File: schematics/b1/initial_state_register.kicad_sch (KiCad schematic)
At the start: 18 parts, among them SW1 SW_SPDT, SW2 SW_SPDT, SW3 SW_SPDT, SW4 SW_SPDT, SW5 SW_SPDT, SW6 SW_SPDT, SW7 SW_SPDT, SW8 SW_Push, U1 74HC165

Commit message: Added schematic page for the status block.
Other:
- company: (none) -> shawnd.xyz
- title: B1 -> Initial State Register
- moved on the sheet: C1
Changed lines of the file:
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@@
   (paper "A4")
   (title_block
-    (title "B1")
-    (date "2024-02-01")
+    (title "Initial State Register")
+    (date "2024-02-05")
     (rev "1")
+    (company "shawnd.xyz")
     (comment 2 "clear EEPROM memory if high at boot time.")
     (comment 3 "configure the unit ID by toggling the DIP switches. There is also a reset button that will")
@@
     (stroke (width 0) (type default))
   )
-  (wire (pts (xy 170.18 34.29) (xy 189.23 34.29))
+  (wire (pts (xy 170.18 34.29) (xy 185.42 34.29))
     (stroke (width 0) (type default))
   )
@@
     (stroke (width 0) (type default))
   )
-  (wire (pts (xy 189.23 43.18) (xy 189.23 44.45))
-    (stroke (width 0) (type default))
-  )
   (wire (pts (xy 125.73 133.35) (xy 138.43 133.35))
     (stroke (width 0) (type default))
@@
     (stroke (width 0) (type default))
   )
-  (wire (pts (xy 189.23 34.29) (xy 189.23 35.56))
+  (wire (pts (xy 185.42 34.29) (xy 185.42 35.56))
     (stroke (width 0) (type default))
   )
@@
     (stroke (width 0) (type default))
   )
-  (wire (pts (xy 102.87 50.8) (xy 102.87 53.34))
+  (wire (pts (xy 102.87 52.07) (xy 102.87 53.34))
     (stroke (width 0) (type default))
   )
@@
     (stroke (width 0) (type default))
   )
-  (wire (pts (xy 105.41 171.45) (xy 105.41 168.91))
+  (wire (pts (xy 105.41 170.18) (xy 105.41 168.91))
     (stroke (width 0) (type default))
   )
@@
     (effects (font (size 1.27 1.27)) (justify left))
   )
-  (hierarchical_label "VCC" (shape input) (at 102.87 50.8 90) (fields_autoplaced)
+  (hierarchical_label "VCC" (shape input) (at 102.87 52.07 90) (fields_autoplaced)
     (effects (font (size 1.27 1.27)) (justify left))
   )
@@
     )
   )
-  (symbol (lib_id "Device:C_Polarized") (at 189.23 39.37 0) (unit 1)
+  (symbol (lib_id "Device:C_Polarized") (at 185.42 39.37 0) (unit 1)
     (in_bom yes) (on_board yes) (dnp no) (fields_autoplaced)
-    (property "Reference" "C1" (at 193.04 37.211 0)
+    (property "Reference" "C1" (at 189.23 37.211 0)
       (effects (font (size 1.27 1.27)) (justify left))
     )
-    (property "Value" "10u" (at 193.04 39.751 0)
+    (property "Value" "10u" (at 189.23 39.751 0)
       (effects (font (size 1.27 1.27)) (justify left))
     )
-    (property "Footprint" "" (at 190.1952 43.18 0)
-      (effects (font (size 1.27 1.27)) hide)
-    )
-    (property "Datasheet" "~" (at 189.23 39.37 0)
+    (property "Footprint" "" (at 186.3852 43.18 0)
+      (effects (font (size 1.27 1.27)) hide)
+    )
+    (property "Datasheet" "~" (at 185.42 39.37 0)
       (effects (font (size 1.27 1.27)) hide)
     )
@@
     )
   )
-  (symbol (lib_id "power:GND") (at 105.41 171.45 0) (unit 1)
+  (symbol (lib_id "power:GND") (at 105.41 170.18 0) (unit 1)
     (in_bom yes) (on_board yes) (dnp no) (fields_autoplaced)
-    (property "Reference" "#PWR03" (at 105.41 177.8 0)
-      (effects (font (size 1.27 1.27)) hide)
-    )
-    (property "Value" "GND" (at 105.41 176.53 0)
-      (effects (font (size 1.27 1.27)))
-    )
-    (property "Footprint" "" (at 105.41 171.45 0)
-      (effects (font (size 1.27 1.27)) hide)
-    )
-    (property "Datasheet" "" (at 105.41 171.45 0)
+    (property "Reference" "#PWR03" (at 105.41 176.53 0)
+      (effects (font (size 1.27 1.27)) hide)
+    )
+    (property "Value" "GND" (at 105.41 175.26 0)
+      (effects (font (size 1.27 1.27)))
+    )
+    (property "Footprint" "" (at 105.41 170.18 0)
+      (effects (font (size 1.27 1.27)) hide)
+    )
+    (property "Datasheet" "" (at 105.41 170.18 0)
       (effects (font (size 1.27 1.27)) hide)
     )
@@
     )
   )
-  (symbol (lib_id "power:GND") (at 189.23 44.45 0) (unit 1)
+  (symbol (lib_id "power:GND") (at 185.42 43.18 0) (unit 1)
     (in_bom yes) (on_board yes) (dnp no) (fields_autoplaced)
-    (property "Reference" "#PWR05" (at 189.23 50.8 0)
-      (effects (font (size 1.27 1.27)) hide)
-    )
-    (property "Value" "GND" (at 189.23 49.53 0)
-      (effects (font (size 1.27 1.27)))
-    )
-    (property "Footprint" "" (at 189.23 44.45 0)
-      (effects (font (size 1.27 1.27)) hide)
-    )
-    (property "Datasheet" "" (at 189.23 44.45 0)
-      (effects (font (size 1.27 1.27)) hide)
-    )
+    (property "Reference" "#PWR05" (at 185.42 49.53 0)
+      (effects (font (size 1.27 1.27)) hide)
+    )
+    (property "Value" "GND" (at 185.42 48.26 0)
+      (effects (font (size 1.27 1.27)))
+    )
+    (property "Footprint" "" (at 185.42 43.18 0)
+      (effects (font (size 1.27 1.27)) hide)
+    )
+    (property "Datasheet" "" (at 185.42 43.18 0)
+      (effects (font (size 1.27 1.27)) hide)
+    )

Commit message: Updated schematics.
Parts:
- added C6: 0.1u, symbol Device:C
- C1: value 10u -> 1u
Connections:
- net GND: now also C6.2
- net VCC: now also C6.1
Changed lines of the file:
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@@
   (junction (at 102.87 146.05) (diameter 0) (color 0 0 0 0)
+  )
+  (junction (at 199.39 44.45) (diameter 0) (color 0 0 0 0)
+  )
+  (junction (at 185.42 34.29) (diameter 0) (color 0 0 0 0)
   )
   (junction (at 102.87 99.06) (diameter 0) (color 0 0 0 0)
@@
     (stroke (width 0) (type default))
   )
+  (wire (pts (xy 199.39 44.45) (xy 199.39 43.18))
+    (stroke (width 0) (type default))
+  )
   (wire (pts (xy 102.87 130.81) (xy 102.87 115.57))
     (stroke (width 0) (type default))
@@
     (stroke (width 0) (type default))
   )
+  (wire (pts (xy 199.39 35.56) (xy 199.39 34.29))
+    (stroke (width 0) (type default))
+  )
   (wire (pts (xy 102.87 53.34) (xy 115.57 53.34))
     (stroke (width 0) (type default))
@@
     (stroke (width 0) (type default))
   )
+  (wire (pts (xy 185.42 44.45) (xy 185.42 43.18))
+    (stroke (width 0) (type default))
+  )
   (wire (pts (xy 105.41 120.65) (xy 106.68 120.65))
     (stroke (width 0) (type default))
@@
     (stroke (width 0) (type default))
   )
+  (wire (pts (xy 185.42 34.29) (xy 199.39 34.29))
+    (stroke (width 0) (type default))
+  )
   (wire (pts (xy 125.73 148.59) (xy 140.97 148.59))
     (stroke (width 0) (type default))
   )
+  (wire (pts (xy 199.39 44.45) (xy 185.42 44.45))
+    (stroke (width 0) (type default))
+  )
   (wire (pts (xy 133.35 101.6) (xy 133.35 63.5))
     (stroke (width 0) (type default))
@@
   )
   (wire (pts (xy 138.43 68.58) (xy 157.48 68.58))
+    (stroke (width 0) (type default))
+  )
+  (wire (pts (xy 199.39 45.72) (xy 199.39 44.45))
     (stroke (width 0) (type default))
   )
@@
       (effects (font (size 1.27 1.27)) (justify left))
     )
-    (property "Value" "10u" (at 189.23 39.751 0)
+    (property "Value" "1u" (at 189.23 39.751 0)
       (effects (font (size 1.27 1.27)) (justify left))
     )
@@
     )
   )
+  (symbol (lib_id "Device:C") (at 199.39 39.37 0) (unit 1)
+    (in_bom yes) (on_board yes) (dnp no) (fields_autoplaced)
+    (property "Reference" "C6" (at 203.2 38.1 0)
+      (effects (font (size 1.27 1.27)) (justify left))
+    )
+    (property "Value" "0.1u" (at 203.2 40.64 0)
+      (effects (font (size 1.27 1.27)) (justify left))
+    )
+    (property "Footprint" "" (at 200.3552 43.18 0)
+      (effects (font (size 1.27 1.27)) hide)
+    )
+    (property "Datasheet" "~" (at 199.39 39.37 0)
+      (effects (font (size 1.27 1.27)) hide)
+    )
+    (pin "2")
+    (pin "1")
+    (instances
+      (project "b1"
+        (path "/d6142fa5-2354-4512-9919-37616259c364/15951702-f191-4c4b-b68c-efdb5de618b5"
+          (reference "C6") (unit 1)
+        )
+      )
+    )
+  )
   (symbol (lib_id "Switch:SW_SPDT") (at 120.65 55.88 0) (mirror y) (unit 1)
     (in_bom yes) (on_board yes) (dnp no)
@@
     )
   )
-  (symbol (lib_id "power:GND") (at 185.42 43.18 0) (unit 1)
+  (symbol (lib_id "power:GND") (at 199.39 45.72 0) (unit 1)
     (in_bom yes) (on_board yes) (dnp no) (fields_autoplaced)
-    (property "Reference" "#PWR05" (at 185.42 49.53 0)
-      (effects (font (size 1.27 1.27)) hide)
-    )
-    (property "Value" "GND" (at 185.42 48.26 0)
-      (effects (font (size 1.27 1.27)))
-    )
-    (property "Footprint" "" (at 185.42 43.18 0)
-      (effects (font (size 1.27 1.27)) hide)
-    )
-    (property "Datasheet" "" (at 185.42 43.18 0)
-      (effects (font (size 1.27 1.27)) hide)
-    )
+    (property "Reference" "#PWR05" (at 199.39 52.07 0)
+      (effects (font (size 1.27 1.27)) hide)
+    )
+    (property "Value" "GND" (at 199.39 50.8 0)
+      (effects (font (size 1.27 1.27)))
+    )
+    (property "Footprint" "" (at 199.39 45.72 0)
+      (effects (font (size 1.27 1.27)) hide)
+    )
+    (property "Datasheet" "" (at 199.39 45.72 0)
+      (effects (font (size 1.27 1.27)) hide)
+    )

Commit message: Updated bypass capacitor values.
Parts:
- added C3: 10u, symbol Device:C_Polarized
- C1: symbol Device:C_Polarized -> Device:C
- renumbered C6 to C2
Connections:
- net GND: now also C3.2
- net VCC: now also C3.1
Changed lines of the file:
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@@
   (junction (at 102.87 115.57) (diameter 0) (color 0 0 0 0)
   )
+  (junction (at 213.36 44.45) (diameter 0) (color 0 0 0 0)
+  )
   (junction (at 102.87 130.81) (diameter 0) (color 0 0 0 0)
   )
@@
   )
   (junction (at 105.41 168.91) (diameter 0) (color 0 0 0 0)
+  )
+  (junction (at 199.39 34.29) (diameter 0) (color 0 0 0 0)
   )
   (junction (at 102.87 68.58) (diameter 0) (color 0 0 0 0)
@@
     (stroke (width 0) (type default))
   )
+  (wire (pts (xy 213.36 43.18) (xy 213.36 44.45))
+    (stroke (width 0) (type default))
+  )
   (wire (pts (xy 170.18 34.29) (xy 185.42 34.29))
     (stroke (width 0) (type default))
@@
     (stroke (width 0) (type default))
   )
+  (wire (pts (xy 213.36 44.45) (xy 199.39 44.45))
+    (stroke (width 0) (type default))
+  )
   (wire (pts (xy 105.41 104.14) (xy 105.41 120.65))
     (stroke (width 0) (type default))
@@
     (stroke (width 0) (type default))
   )
-  (wire (pts (xy 199.39 45.72) (xy 199.39 44.45))
+  (wire (pts (xy 213.36 45.72) (xy 213.36 44.45))
     (stroke (width 0) (type default))
   )
@@
     (stroke (width 0) (type default))
   )
+  (wire (pts (xy 213.36 35.56) (xy 213.36 34.29))
+    (stroke (width 0) (type default))
+  )
   (wire (pts (xy 102.87 146.05) (xy 115.57 146.05))
     (stroke (width 0) (type default))
@@
   )
   (wire (pts (xy 105.41 58.42) (xy 105.41 73.66))
+    (stroke (width 0) (type default))
+  )
+  (wire (pts (xy 213.36 34.29) (xy 199.39 34.29))
     (stroke (width 0) (type default))
   )
@@
   (symbol (lib_id "power:GND") (at 170.18 93.98 0) (unit 1)
     (in_bom yes) (on_board yes) (dnp no) (fields_autoplaced)
-    (property "Reference" "#PWR04" (at 170.18 100.33 0)
+    (property "Reference" "#PWR02" (at 170.18 100.33 0)
       (effects (font (size 1.27 1.27)) hide)
     )
@@
       (project "b1"
         (path "/d6142fa5-2354-4512-9919-37616259c364/15951702-f191-4c4b-b68c-efdb5de618b5"
-          (reference "#PWR04") (unit 1)
+          (reference "#PWR02") (unit 1)
         )
       )
@@
     )
   )
-  (symbol (lib_id "Device:C_Polarized") (at 185.42 39.37 0) (unit 1)
+  (symbol (lib_id "Device:C") (at 185.42 39.37 0) (unit 1)
     (in_bom yes) (on_board yes) (dnp no) (fields_autoplaced)
-    (property "Reference" "C1" (at 189.23 37.211 0)
+    (property "Reference" "C1" (at 189.23 38.1 0)
       (effects (font (size 1.27 1.27)) (justify left))
     )
-    (property "Value" "1u" (at 189.23 39.751 0)
+    (property "Value" "1u" (at 189.23 40.64 0)
       (effects (font (size 1.27 1.27)) (justify left))
     )
@@
   (symbol (lib_id "power:GND") (at 105.41 170.18 0) (unit 1)
     (in_bom yes) (on_board yes) (dnp no) (fields_autoplaced)
-    (property "Reference" "#PWR03" (at 105.41 176.53 0)
+    (property "Reference" "#PWR01" (at 105.41 176.53 0)
       (effects (font (size 1.27 1.27)) hide)
     )
@@
       (project "b1"
         (path "/d6142fa5-2354-4512-9919-37616259c364/15951702-f191-4c4b-b68c-efdb5de618b5"
-          (reference "#PWR03") (unit 1)
+          (reference "#PWR01") (unit 1)
         )
       )
@@
   (symbol (lib_id "Device:C") (at 199.39 39.37 0) (unit 1)
     (in_bom yes) (on_board yes) (dnp no) (fields_autoplaced)
-    (property "Reference" "C6" (at 203.2 38.1 0)
+    (property "Reference" "C2" (at 203.2 38.1 0)
       (effects (font (size 1.27 1.27)) (justify left))
     )
@@
       (project "b1"
         (path "/d6142fa5-2354-4512-9919-37616259c364/15951702-f191-4c4b-b68c-efdb5de618b5"
-          (reference "C6") (unit 1)
+          (reference "C2") (unit 1)
         )
       )
@@
     )
   )
-  (symbol (lib_id "power:GND") (at 199.39 45.72 0) (unit 1)
+  (symbol (lib_id "power:GND") (at 213.36 45.72 0) (unit 1)
     (in_bom yes) (on_board yes) (dnp no) (fields_autoplaced)
-    (property "Reference" "#PWR05" (at 199.39 52.07 0)
-      (effects (font (size 1.27 1.27)) hide)
-    )
-    (property "Value" "GND" (at 199.39 50.8 0)
-      (effects (font (size 1.27 1.27)))
-    )
-    (property "Footprint" "" (at 199.39 45.72 0)
-      (effects (font (size 1.27 1.27)) hide)
-    )
-    (property "Datasheet" "" (at 199.39 45.72 0)
-      (effects (font (size 1.27 1.27)) hide)
-    )
-    (pin "1")
-    (instances
-      (project "b1"
-        (path "/d6142fa5-2354-4512-9919-37616259c364/15951702-f191-4c4b-b68c-efdb5de618b5"
-          (reference "#PWR05") (unit 1)
+    (property "Reference" "#PWR03" (at 213.36 52.07 0)
+      (effects (font (size 1.27 1.27)) hide)
+    )
+    (property "Value" "GND" (at 213.36 50.8 0)
+      (effects (font (size 1.27 1.27)))
+    )
+    (property "Footprint" "" (at 213.36 45.72 0)
+      (effects (font (size 1.27 1.27)) hide)
+    )
+    (property "Datasheet" "" (at 213.36 45.72 0)
+      (effects (font (size 1.27 1.27)) hide)
+    )
+    (pin "1")
+    (instances
+      (project "b1"
+        (path "/d6142fa5-2354-4512-9919-37616259c364/15951702-f191-4c4b-b68c-efdb5de618b5"
+          (reference "#PWR03") (unit 1)
         )
       )
@@
         )
       )
+    )
+  )
+  (symbol (lib_id "Device:C_Polarized") (at 213.36 39.37 0) (unit 1)
+    (in_bom yes) (on_board yes) (dnp no)
+    (property "Reference" "C3" (at 217.17 38.1 0)
+      (effects (font (size 1.27 1.27)) (justify left))
+    )
+    (property "Value" "10u" (at 217.17 40.64 0)
+      (effects (font (size 1.27 1.27)) (justify left))
+    )
+    (property "Footprint" "" (at 214.3252 43.18 0)
+      (effects (font (size 1.27 1.27)) hide)
+    )
+    (property "Datasheet" "~" (at 213.36 39.37 0)
+      (effects (font (size 1.27 1.27)) hide)
+    )
+    (pin "2")
+    (pin "1")
+    (instances
+      (project "b1"
+        (path "/d6142fa5-2354-4512-9919-37616259c364/15951702-f191-4c4b-b68c-efdb5de618b5"
+          (reference "C3") (unit 1)
+        )
+      )

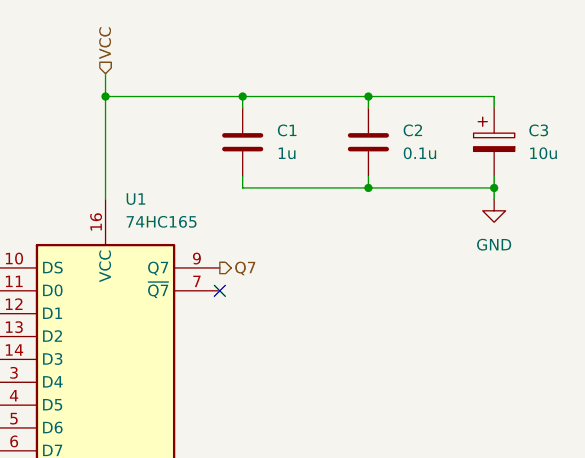
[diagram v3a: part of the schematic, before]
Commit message: Added schematic page for LoRa.
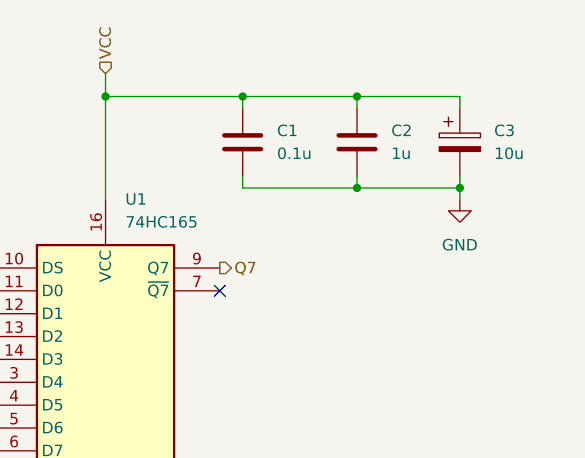
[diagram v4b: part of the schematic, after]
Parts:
- C1: value 1u -> 0.1u
- C2: value 0.1u -> 1u
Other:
- moved on the sheet: C2, C3
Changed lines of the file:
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@@
   (title_block
     (title "Initial State Register")
-    (date "2024-02-05")
+    (date "2024-02-06")
     (rev "1")
     (company "shawnd.xyz")
@@
     (comment 4 "The initial state register is used to read a B1 unit's ID upon first boot. The user can")
   )
+  (junction (at 198.12 44.45) (diameter 0) (color 0 0 0 0)
+  )
   (junction (at 105.41 73.66) (diameter 0) (color 0 0 0 0)
   )
   (junction (at 102.87 53.34) (diameter 0) (color 0 0 0 0)
   )
+  (junction (at 209.55 44.45) (diameter 0) (color 0 0 0 0)
+  )
   (junction (at 105.41 151.13) (diameter 0) (color 0 0 0 0)
   )
+  (junction (at 198.12 34.29) (diameter 0) (color 0 0 0 0)
+  )
   (junction (at 102.87 115.57) (diameter 0) (color 0 0 0 0)
   )
-  (junction (at 213.36 44.45) (diameter 0) (color 0 0 0 0)
-  )
   (junction (at 102.87 130.81) (diameter 0) (color 0 0 0 0)
   )
@@
   (junction (at 102.87 146.05) (diameter 0) (color 0 0 0 0)
   )
-  (junction (at 199.39 44.45) (diameter 0) (color 0 0 0 0)
-  )
   (junction (at 185.42 34.29) (diameter 0) (color 0 0 0 0)
   )
@@
   )
   (junction (at 105.41 168.91) (diameter 0) (color 0 0 0 0)
-  )
-  (junction (at 199.39 34.29) (diameter 0) (color 0 0 0 0)
   )
   (junction (at 102.87 68.58) (diameter 0) (color 0 0 0 0)
@@
     (stroke (width 0) (type default))
   )
-  (wire (pts (xy 199.39 44.45) (xy 199.39 43.18))
+  (wire (pts (xy 198.12 44.45) (xy 198.12 43.18))
     (stroke (width 0) (type default))
   )
@@
     (stroke (width 0) (type default))
   )
-  (wire (pts (xy 213.36 43.18) (xy 213.36 44.45))
+  (wire (pts (xy 209.55 43.18) (xy 209.55 44.45))
     (stroke (width 0) (type default))
   )
@@
     (stroke (width 0) (type default))
   )
-  (wire (pts (xy 199.39 35.56) (xy 199.39 34.29))
+  (wire (pts (xy 198.12 35.56) (xy 198.12 34.29))
     (stroke (width 0) (type default))
   )
@@
     (stroke (width 0) (type default))
   )
+  (wire (pts (xy 198.12 44.45) (xy 209.55 44.45))
+    (stroke (width 0) (type default))
+  )
   (wire (pts (xy 127 168.91) (xy 127 163.83))
     (stroke (width 0) (type default))
@@
     (stroke (width 0) (type default))
   )
-  (wire (pts (xy 213.36 44.45) (xy 199.39 44.45))
-    (stroke (width 0) (type default))
-  )
   (wire (pts (xy 105.41 104.14) (xy 105.41 120.65))
     (stroke (width 0) (type default))
@@
     (stroke (width 0) (type default))
   )
-  (wire (pts (xy 185.42 34.29) (xy 199.39 34.29))
+  (wire (pts (xy 185.42 34.29) (xy 198.12 34.29))
     (stroke (width 0) (type default))
   )
@@
     (stroke (width 0) (type default))
   )
-  (wire (pts (xy 199.39 44.45) (xy 185.42 44.45))
-    (stroke (width 0) (type default))
-  )
   (wire (pts (xy 133.35 101.6) (xy 133.35 63.5))
     (stroke (width 0) (type default))
@@
     (stroke (width 0) (type default))
   )
-  (wire (pts (xy 213.36 45.72) (xy 213.36 44.45))
+  (wire (pts (xy 209.55 45.72) (xy 209.55 44.45))
+    (stroke (width 0) (type default))
+  )
+  (wire (pts (xy 198.12 44.45) (xy 185.42 44.45))
     (stroke (width 0) (type default))
   )
@@
     (stroke (width 0) (type default))
   )
-  (wire (pts (xy 213.36 35.56) (xy 213.36 34.29))
+  (wire (pts (xy 209.55 35.56) (xy 209.55 34.29))
     (stroke (width 0) (type default))
   )
@@
     (stroke (width 0) (type default))
   )
-  (wire (pts (xy 213.36 34.29) (xy 199.39 34.29))
+  (wire (pts (xy 198.12 34.29) (xy 209.55 34.29))
     (stroke (width 0) (type default))
   )
@@
       (effects (font (size 1.27 1.27)) (justify left))
     )
-    (property "Value" "1u" (at 189.23 40.64 0)
+    (property "Value" "0.1u" (at 189.23 40.64 0)
       (effects (font (size 1.27 1.27)) (justify left))
     )
@@
     )
   )
-  (symbol (lib_id "Device:C") (at 199.39 39.37 0) (unit 1)
+  (symbol (lib_id "Device:C") (at 198.12 39.37 0) (unit 1)
     (in_bom yes) (on_board yes) (dnp no) (fields_autoplaced)
-    (property "Reference" "C2" (at 203.2 38.1 0)
+    (property "Reference" "C2" (at 201.93 38.1 0)
       (effects (font (size 1.27 1.27)) (justify left))
     )
-    (property "Value" "0.1u" (at 203.2 40.64 0)
+    (property "Value" "1u" (at 201.93 40.64 0)
       (effects (font (size 1.27 1.27)) (justify left))
     )
-    (property "Footprint" "" (at 200.3552 43.18 0)
-      (effects (font (size 1.27 1.27)) hide)
-    )
-    (property "Datasheet" "~" (at 199.39 39.37 0)
+    (property "Footprint" "" (at 199.0852 43.18 0)
+      (effects (font (size 1.27 1.27)) hide)
+    )
+    (property "Datasheet" "~" (at 198.12 39.37 0)
       (effects (font (size 1.27 1.27)) hide)
     )
@@
     )
   )
-  (symbol (lib_id "power:GND") (at 213.36 45.72 0) (unit 1)
+  (symbol (lib_id "power:GND") (at 209.55 45.72 0) (unit 1)
     (in_bom yes) (on_board yes) (dnp no) (fields_autoplaced)
-    (property "Reference" "#PWR03" (at 213.36 52.07 0)
-      (effects (font (size 1.27 1.27)) hide)
-    )
-    (property "Value" "GND" (at 213.36 50.8 0)
-      (effects (font (size 1.27 1.27)))
-    )
-    (property "Footprint" "" (at 213.36 45.72 0)
-      (effects (font (size 1.27 1.27)) hide)
-    )
-    (property "Datasheet" "" (at 213.36 45.72 0)
+    (property "Reference" "#PWR03" (at 209.55 52.07 0)
+      (effects (font (size 1.27 1.27)) hide)
+    )
+    (property "Value" "GND" (at 209.55 50.8 0)
+      (effects (font (size 1.27 1.27)))
+    )
+    (property "Footprint" "" (at 209.55 45.72 0)
+      (effects (font (size 1.27 1.27)) hide)
+    )
+    (property "Datasheet" "" (at 209.55 45.72 0)
       (effects (font (size 1.27 1.27)) hide)
     )
@@
     )
   )
-  (symbol (lib_id "Device:C_Polarized") (at 213.36 39.37 0) (unit 1)
-    (in_bom yes) (on_board yes) (dnp no)
-    (property "Reference" "C3" (at 217.17 38.1 0)
+  (symbol (lib_id "Device:C_Polarized") (at 209.55 39.37 0) (unit 1)
+    (in_bom yes) (on_board yes) (dnp no)
+    (property "Reference" "C3" (at 213.36 38.1 0)
       (effects (font (size 1.27 1.27)) (justify left))
     )
-    (property "Value" "10u" (at 217.17 40.64 0)
+    (property "Value" "10u" (at 213.36 40.64 0)
       (effects (font (size 1.27 1.27)) (justify left))
     )
-    (property "Footprint" "" (at 214.3252 43.18 0)
-      (effects (font (size 1.27 1.27)) hide)
-    )
-    (property "Datasheet" "~" (at 213.36 39.37 0)
-      (effects (font (size 1.27 1.27)) hide)
-    )
+    (property "Footprint" "" (at 210.5152 43.18 0)
+      (effects (font (size 1.27 1.27)) hide)
+    )
+    (property "Datasheet" "~" (at 209.55 39.37 0)
+      (effects (font (size 1.27 1.27)) hide)
+    )

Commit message: Updated labels.
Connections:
- net PL renamed ~{PL}
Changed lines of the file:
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@@
     (effects (font (size 1.27 1.27)) (justify left bottom))
   )
-  (hierarchical_label "PL" (shape input) (at 157.48 78.74 180) (fields_autoplaced)
+  (hierarchical_label "~{PL}" (shape input) (at 157.48 78.74 180) (fields_autoplaced)
     (effects (font (size 1.27 1.27)) (justify right))
   )
